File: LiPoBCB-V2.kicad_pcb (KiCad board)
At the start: 2 copper layers, 30 x 16.5 mm, 27 parts, among them J1 USB-C_6_pin_receptacle, J2 Conn_01x02, Q1 Q_Dual_PMOS_S1G1D2S2G2D1, U1 ETA9740

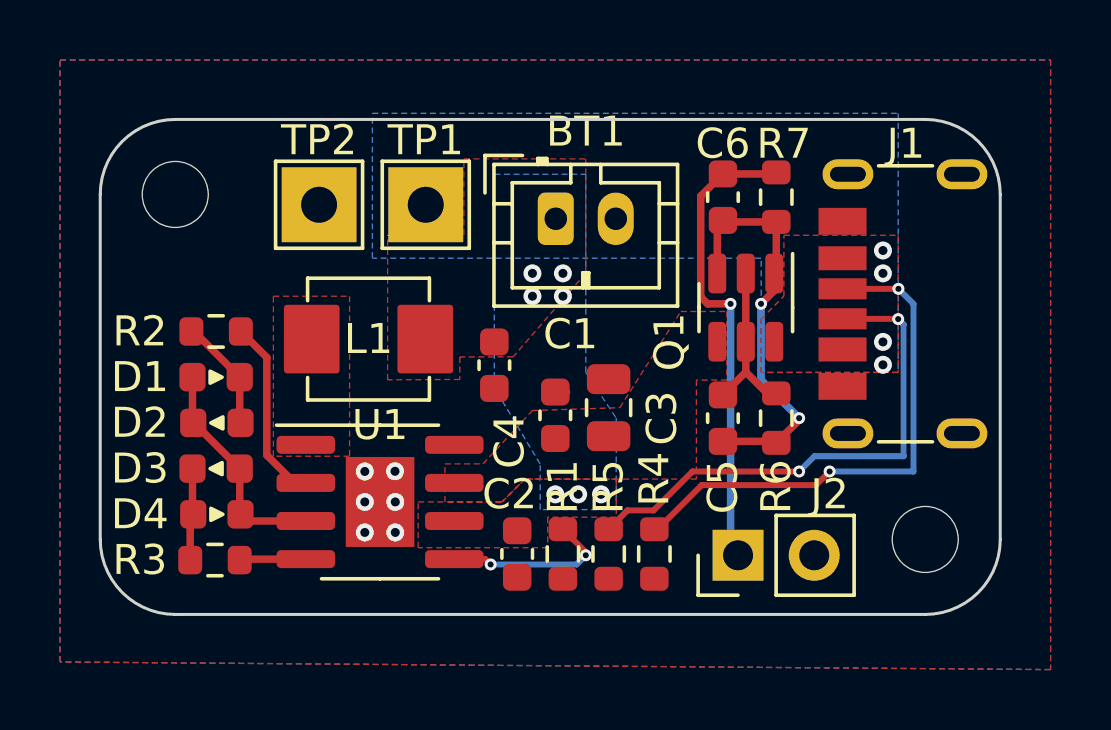
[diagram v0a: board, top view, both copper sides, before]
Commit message: DRC no errors
added 3d models
switched q1a and q1b
optimized polygons
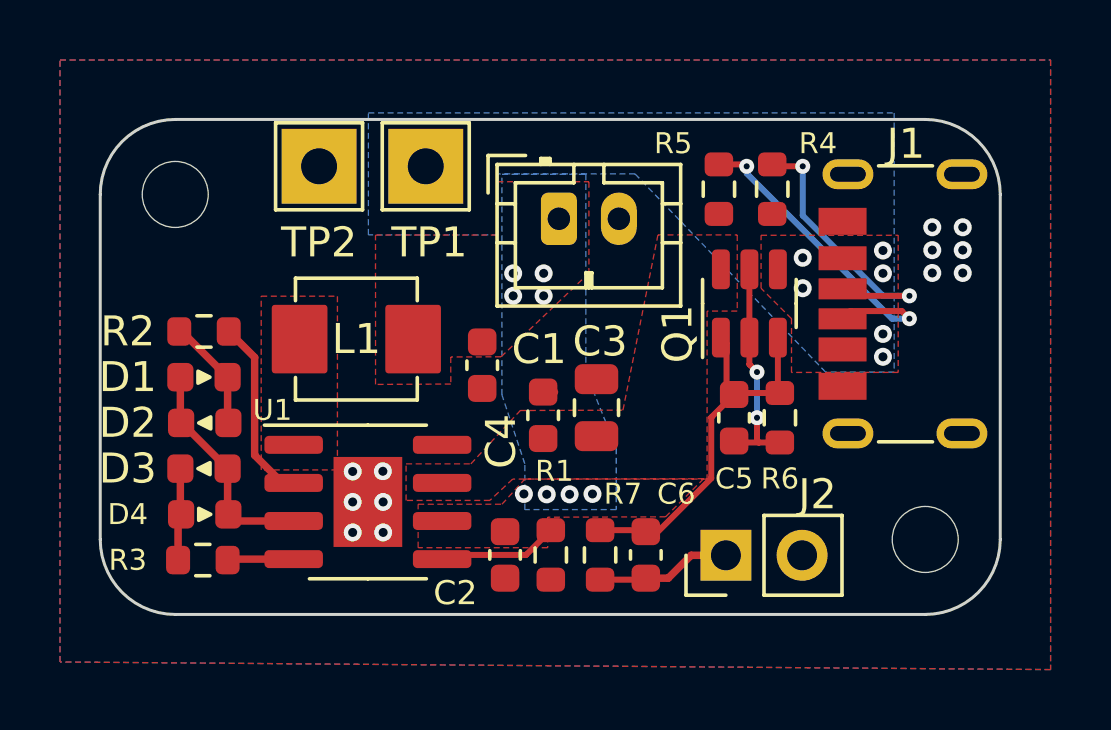
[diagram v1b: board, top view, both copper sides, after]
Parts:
- moved R7 13.3 mm to (146.7, 64.5), turned to -90 degrees
- moved R4 12.8 mm to (152.4, 52.3)
- moved R5 12.7 mm to (150.6, 52.3)
- moved C6 12.2 mm to (148.2, 64.5), turned to -90 degrees
- moved TP1 1.28 mm to (140.9, 51.6)
- moved TP2 1.28 mm to (137.3, 51.6)
- moved C2 0.41 mm to (143.5, 64.5)
- moved R1 0.41 mm to (145.0, 64.5)
- moved C3 0.40 mm to (146.5, 59.6)
- moved C4 0.40 mm to (142.7, 58.2)
- moved D2 0.40 mm to (133.5, 60.1)
- moved D4 0.40 mm to (133.5, 63.2)
- moved J2 0.40 mm to (150.9, 64.5)
- moved L1 0.40 mm to (138.5, 57.3)
- moved R3 0.40 mm to (133.4, 64.7)
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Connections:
- Q1 pad 4: +5V -> /VBUS
- Q1 pad 6: /VBUS -> +5V
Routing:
- net Net-(C6-Pad2): track 16.0 -> 4.53 mm, vias 1 -> 0
- net /CC2: track 17.6 -> 9.67 mm
- net /CC1: track 17.3 -> 11.1 mm
- net Net-(C5-Pad1): track 5.67 -> 7.45 mm, vias 0 -> 2
- net /ISET: track 5.77 -> 4.02 mm, vias 2 -> 0
- net /SW_GATE: track 13.9 -> 12.7 mm, vias 2 -> 0
- net GND: track 1.24 -> 0.37 mm, vias 6 -> 12
- net /VBUS: track 0.36 -> 0.00 mm, vias 4 -> 6
- net /BAT: track 0.35 -> 0.02 mm, vias 7 -> 8

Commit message: Updates design rules
edited inductor footprint
removed custom design rules
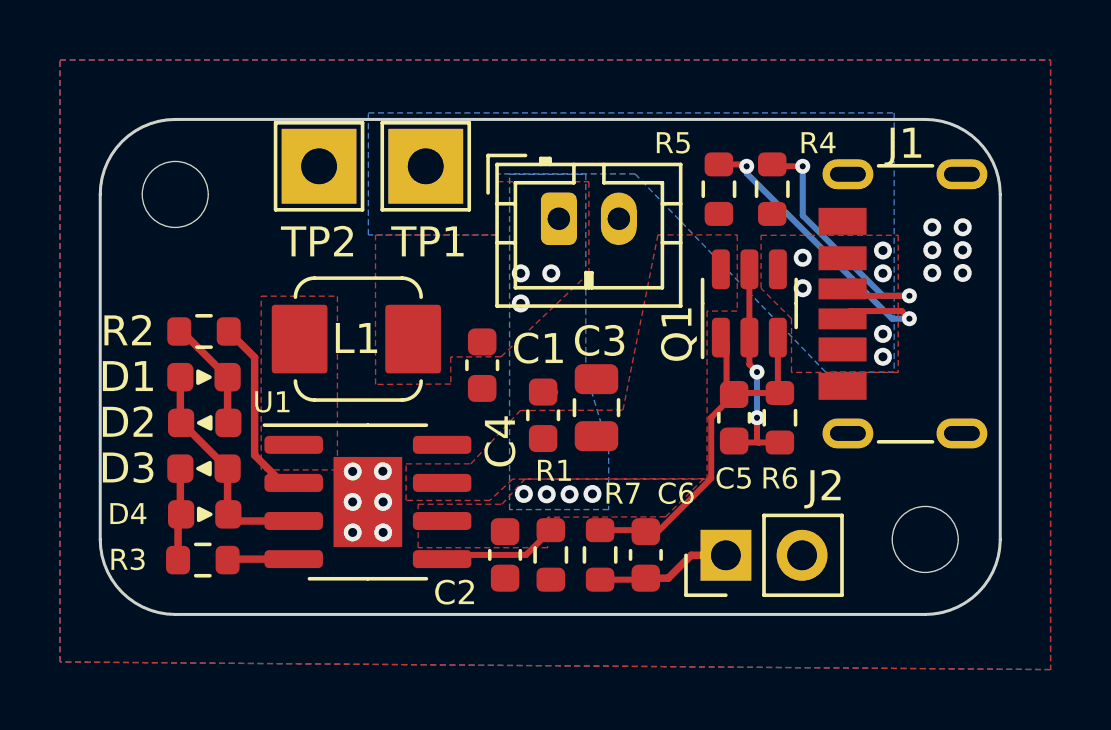
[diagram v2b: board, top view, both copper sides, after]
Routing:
- net /BAT: vias 8 -> 7
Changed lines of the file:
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@@
     (property "Sheetname" "")
     (attr through_hole)
-    (fp_text reference "J2" (at 2.032 3.053 180) (layer "F.SilkS")
+    (fp_text reference "J2" (at 2.298478 3.323 180) (layer "F.SilkS")
       (effects (font (size 1 1) (thickness 0.15)))
     )
@@
       (effects (font (size 1 1) (thickness 0.15)))
     )
-    (fp_line (start 2.03 2.03) (end 2.03 1.28) (layer "F.SilkS") (width 0.12))
-    (fp_line (start 2.03 -2.03) (end 2.03 -1.28) (layer "F.SilkS") (width 0.12))
-    (fp_line (start -2.03 2.03) (end -2.03 1.28) (layer "F.SilkS") (width 0.12))
-    (fp_line (start -2.03 -2.03) (end -2.03 -1.28) (layer "F.SilkS") (width 0.12))
-    (fp_line (start -2.03 2.03) (end 2.03 2.03) (layer "F.SilkS") (width 0.12))
-    (fp_line (start -2.03 -2.03) (end 2.03 -2.03) (layer "F.SilkS") (width 0.12))
+    (fp_line (start 1.524 2.032) (end -1.397 2.032) (layer "F.SilkS") (width 0.12))
+    (fp_line (start -1.397 -2.032) (end 1.524 -2.032) (layer "F.SilkS") (width 0.12))
+    (fp_arc (start 1.524 -2.032) (mid 1.973013 -1.846013) (end 2.159 -1.397) (layer "F.SilkS") (width 0.12))
+    (fp_arc (start 2.159 1.397) (mid 1.973013 1.846013) (end 1.524 2.032) (layer "F.SilkS") (width 0.12))
+    (fp_arc (start -2.032 -1.397) (mid -1.846013 -1.846013) (end -1.397 -2.032) (layer "F.SilkS") (width 0.12))
+    (fp_arc (start -1.397 2.032) (mid -1.846013 1.846013) (end -2.032 1.397) (layer "F.SilkS") (width 0.12))
     (fp_rect (start -3.175 -2.54) (end 3.175 2.54) (layer "F.CrtYd") (width 0.05) (fill none))
     (pad "1" smd roundrect (at -1.89225 0) (size 1.8545 2.286) (layers "F.Cu" "F.Paste" "F.Mask") (roundrect_rratio 0.05392289027)
@@
     (property "Sheetname" "")
     (attr smd)
-    (fp_text reference "U1" (at -3.182478 -3.060478) (layer "F.SilkS")
+    (fp_text reference "U1" (at -3.182478 -3.314478) (layer "F.SilkS")
       (effects (font (size 0.7 0.7) (thickness 0.15)))
     )
@@
   (segment (start 146.84075 60.636478) (end 146.91975 60.557478) (width 0.25) (layer "F.Cu") (net 3))
   (segment (start 142.745 57.670478) (end 142.732 57.657478) (width 0.25) (layer "F.Cu") (net 4))
-  (via (at 144.78 55.88) (size 0.6) (drill 0.3) (layers "F.Cu" "B.Cu") (free) (net 4))
   (via (at 144.121522 62.484) (size 0.6) (drill 0.3) (layers "F.Cu" "B.Cu") (free) (net 4))
-  (via (at 143.764 55.130478) (size 0.6) (drill 0.3) (layers "F.Cu" "B.Cu") (free) (net 4))
-  (via (at 144.78 55.130478) (size 0.6) (drill 0.3) (layers "F.Cu" "B.Cu") (free) (net 4))
-  (via (at 143.764 55.88) (size 0.6) (drill 0.3) (layers "F.Cu" "B.Cu") (free) (net 4))
+  (via (at 144.018 55.130478) (size 0.6) (drill 0.3) (layers "F.Cu" "B.Cu") (free) (net 4))
+  (via (at 145.034 55.130478) (size 0.6) (drill 0.3) (layers "F.Cu" "B.Cu") (free) (net 4))
+  (via (at 144.018 56.134) (size 0.6) (drill 0.3) (layers "F.Cu" "B.Cu") (free) (net 4))
   (via (at 146.407522 62.484) (size 0.6) (drill 0.3) (layers "F.Cu" "B.Cu") (free) (net 4))
   (via (at 145.645522 62.496478) (size 0.6) (drill 0.3) (layers "F.Cu" "B.Cu") (free) (net 4))
@@
       (pts
         (xy 146.184478 58.432478)
-        (xy 147.200478 60.96)
-        (xy 147.200478 63.004478)
-        (xy 144.152478 63.004478)
-        (xy 144.152478 61.480478)
-        (xy 143.390478 59.182)
-        (xy 143.390478 51.828478)
+        (xy 146.946478 60.96)
+        (xy 146.946478 63.004478)
+        (xy 143.644478 63.004478)
+        (xy 143.644478 61.480478)
+        (xy 143.644478 59.182)
+        (xy 143.644478 51.828478)
         (xy 146.184478 51.828478)
       )

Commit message: Adds new solder connector footprints
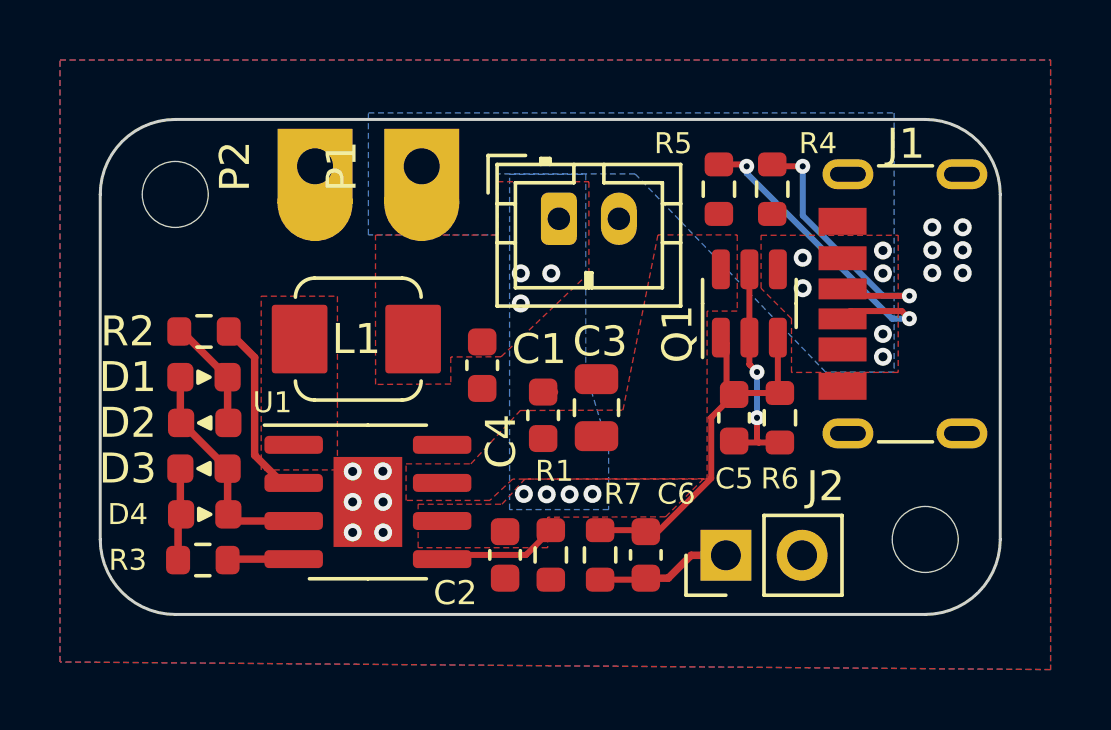
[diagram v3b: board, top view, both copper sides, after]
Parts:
- removed TP1: 5V, TestPoint:TestPoint_THTPad_2.5x2.5mm_Drill1.2mm
- removed TP2: GND, TestPoint:TestPoint_THTPad_2.5x2.5mm_Drill1.2mm
- added P1: Solder Pad, LiPoBCB-V2:TestPoint_THTPad_2.5x2.5mm_Drill1.2mm, F.Cu at (140.7, 51.6)
- added P2: Solder Pad, LiPoBCB-V2:TestPoint_THTPad_2.5x2.5mm_Drill1.2mm, F.Cu at (137.2, 51.6)
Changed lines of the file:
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@@
     )
-  )
-  (footprint "TestPoint:TestPoint_THTPad_2.5x2.5mm_Drill1.2mm" (layer "F.Cu")
-    (at 137.294478 51.562)
-    (descr "THT rectangular pad as test Point, square 2.5mm side length, hole diameter 1.2mm")
-    (tags "test point THT pad rectangle square")
-    (property "Sheetfile" "LiPoBCB-V2.kicad_sch")
-    (property "Sheetname" "")
-    (attr exclude_from_pos_files)
-    (fp_text reference "TP2" (at 0 2.54 180) (layer "F.SilkS")
-      (effects (font (size 1 1) (thickness 0.15)))
-    )
-    (fp_text value "GND" (at 0 2.25) (layer "F.Fab")
-      (effects (font (size 1 1) (thickness 0.15)))
-    )
-    (fp_text user "${REFERENCE}" (at 0 -2.15) (layer "F.Fab")
-      (effects (font (size 1 1) (thickness 0.15)))
-    )
-    (fp_line (start 1.45 -1.45) (end 1.45 1.45) (layer "F.SilkS") (width 0.12))
-    (fp_line (start -1.45 1.45) (end -1.45 -1.45) (layer "F.SilkS") (width 0.12))
-    (fp_line (start -1.45 -1.45) (end 1.45 -1.45) (layer "F.SilkS") (width 0.12))
-    (fp_line (start 1.45 1.45) (end -1.45 1.45) (layer "F.SilkS") (width 0.12))
-    (fp_line (start 1.75 1.75) (end -1.75 1.75) (layer "F.CrtYd") (width 0.05))
-    (fp_line (start -1.75 -1.75) (end 1.75 -1.75) (layer "F.CrtYd") (width 0.05))
-    (fp_line (start -1.75 -1.75) (end -1.75 1.75) (layer "F.CrtYd") (width 0.05))
-    (fp_line (start 1.75 1.75) (end 1.75 -1.75) (layer "F.CrtYd") (width 0.05))
-    (pad "1" thru_hole rect (at 0 0) (size 2.5 2.5) (drill 1.2) (layers *.Cu *.Mask)
-      (net 1 "GND") (pinfunction "1") (pintype "passive"))
   )
   (footprint "LiPoBCB-V2:D_0603_1608Metric" (layer "F.Cu")
@@
       (rotate (xyz 0 0 0))
     )
+  )
+  (footprint "LiPoBCB-V2:TestPoint_THTPad_2.5x2.5mm_Drill1.2mm" (layer "F.Cu")
+    (at 137.16 51.562)
+    (descr "THT rectangular pad as test Point, square 2.5mm side length, hole diameter 1.2mm")
+    (tags "test point THT pad rectangle square")
+    (property "Sheetfile" "LiPoBCB-V2.kicad_sch")
+    (property "Sheetname" "")
+    (attr exclude_from_pos_files)
+    (fp_text reference "P2" (at -2.667 0 270) (layer "F.SilkS")
+      (effects (font (size 1 1) (thickness 0.15)))
+    )
+    (fp_text value "Solder Pad" (at 0 5.08) (layer "F.Fab")
+      (effects (font (size 1 1) (thickness 0.15)))
+    )
+    (fp_text user "${REFERENCE}" (at -2.667 0 270) (layer "F.Fab")
+      (effects (font (size 1 1) (thickness 0.15)))
+    )
+    (fp_line (start -1.524 -1.524) (end 1.524 -1.524) (layer "F.CrtYd") (width 0.05))
+    (fp_line (start 1.524 1.239776) (end 1.524 -1.524) (layer "F.CrtYd") (width 0.05))
+    (fp_line (start -1.524 -1.524) (end -1.524034 1.25) (layer "F.CrtYd") (width 0.05))
+    (fp_arc (start 1.524 1.239776) (mid 0.005112 2.774026) (end -1.524034 1.25) (layer "F.CrtYd") (width 0.05))
+    (pad "1" thru_hole custom (at 0 0) (size 2.5 2.5) (drill 1.2) (layers *.Cu *.Mask)
+      (net 1 "GND") (pinfunction "1") (pintype "passive")
+      (options (clearance outline) (anchor rect))
+      (primitives
+        (gr_circle (center 0 1.24) (end 1.24 1.24) (width 0.02) (fill yes))
+      ))
   )
   (footprint "LiPoBCB-V2:D_0603_1608Metric" (layer "F.Cu")
@@
     )
   )
-  (footprint "TestPoint:TestPoint_THTPad_2.5x2.5mm_Drill1.2mm" (layer "F.Cu")
-    (at 140.850478 51.562)
-    (descr "THT rectangular pad as test Point, square 2.5mm side length, hole diameter 1.2mm")
-    (tags "test point THT pad rectangle square")
-    (property "Sheetfile" "LiPoBCB-V2.kicad_sch")
-    (property "Sheetname" "")
-    (attr exclude_from_pos_files)
-    (fp_text reference "TP1" (at 0.119522 2.54) (layer "F.SilkS")
-      (effects (font (size 1 1) (thickness 0.15)))
-    )
-    (fp_text value "5V" (at 0 2.25) (layer "F.Fab")
-      (effects (font (size 1 1) (thickness 0.15)))
-    )
-    (fp_text user "${REFERENCE}" (at 0 -2.15) (layer "F.Fab")
-      (effects (font (size 1 1) (thickness 0.15)))
-    )
-    (fp_line (start 1.45 1.45) (end -1.45 1.45) (layer "F.SilkS") (width 0.12))
-    (fp_line (start 1.45 -1.45) (end 1.45 1.45) (layer "F.SilkS") (width 0.12))
-    (fp_line (start -1.45 -1.45) (end 1.45 -1.45) (layer "F.SilkS") (width 0.12))
-    (fp_line (start -1.45 1.45) (end -1.45 -1.45) (layer "F.SilkS") (width 0.12))
-    (fp_line (start 1.75 1.75) (end 1.75 -1.75) (layer "F.CrtYd") (width 0.05))
-    (fp_line (start -1.75 -1.75) (end 1.75 -1.75) (layer "F.CrtYd") (width 0.05))
-    (fp_line (start 1.75 1.75) (end -1.75 1.75) (layer "F.CrtYd") (width 0.05))
-    (fp_line (start -1.75 -1.75) (end -1.75 1.75) (layer "F.CrtYd") (width 0.05))
-    (pad "1" thru_hole rect (at 0 0) (size 2.5 2.5) (drill 1.2) (layers *.Cu *.Mask)
-      (net 16 "/VBUS") (pinfunction "1") (pintype "passive"))
-  )
   (footprint "Capacitor_SMD:C_0805_2012Metric" (layer "F.Cu")
     (at 146.542 59.607478 90)
@@
     )
   )
+  (footprint "LiPoBCB-V2:TestPoint_THTPad_2.5x2.5mm_Drill1.2mm" (layer "F.Cu")
+    (at 140.716 51.562)
+    (descr "THT rectangular pad as test Point, square 2.5mm side length, hole diameter 1.2mm")
+    (tags "test point THT pad rectangle square")
+    (property "Sheetfile" "LiPoBCB-V2.kicad_sch")
+    (property "Sheetname" "")
+    (attr exclude_from_pos_files)
+    (fp_text reference "P1" (at -2.667 0 270) (layer "F.SilkS")
+      (effects (font (size 1 1) (thickness 0.15)))
+    )
+    (fp_text value "Solder Pad" (at 0 5.08) (layer "F.Fab")
+      (effects (font (size 1 1) (thickness 0.15)))
+    )
+    (fp_text user "${REFERENCE}" (at -2.667 0 270) (layer "F.Fab")
+      (effects (font (size 1 1) (thickness 0.15)))
+    )
+    (fp_line (start -1.524 -1.524) (end 1.524 -1.524) (layer "F.CrtYd") (width 0.05))
+    (fp_line (start 1.524 1.239776) (end 1.524 -1.524) (layer "F.CrtYd") (width 0.05))
+    (fp_line (start -1.524 -1.524) (end -1.524034 1.25) (layer "F.CrtYd") (width 0.05))
+    (fp_arc (start 1.524 1.239776) (mid 0.005112 2.774026) (end -1.524034 1.25) (layer "F.CrtYd") (width 0.05))
+    (pad "1" thru_hole custom (at 0 0) (size 2.5 2.5) (drill 1.2) (layers *.Cu *.Mask)
+      (net 16 "/VBUS") (pinfunction "1") (pintype "passive")
+      (options (clearance outline) (anchor rect))
+      (primitives
+        (gr_circle (center 0 1.24) (end 1.24 1.24) (width 0.02) (fill yes))
+      ))
+  )
   (footprint "LiPoBCB-V2:L_smd_1616" (layer "F.Cu")

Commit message: Adds silkscreen to the back
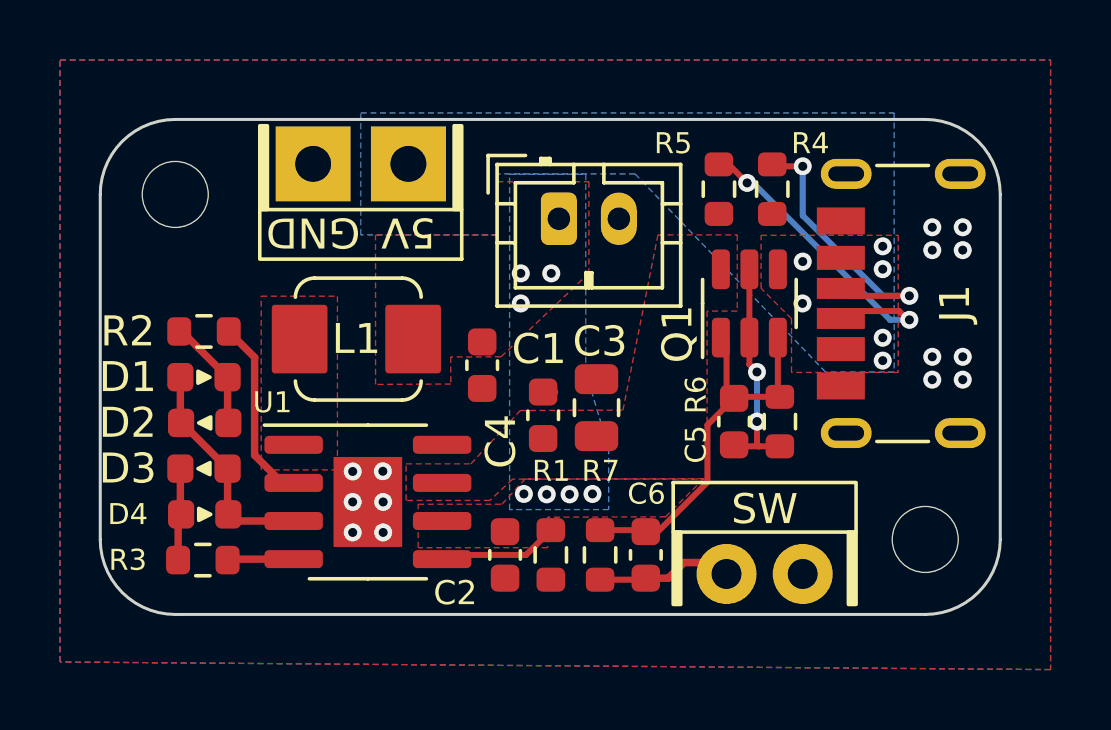
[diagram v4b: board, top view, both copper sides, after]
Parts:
- removed P2: Solder Pad, LiPoBCB-V2:TestPoint_THTPad_2.5x2.5mm_Drill1.2mm
- J2: footprint Connector_PinHeader_2.54mm:PinHeader_1x02_P2.54mm_Vertical -> LiPoBCB-V2:Solder_Connector_SW
- P1: value Solder Pad -> Solder_Connector_X2; footprint LiPoBCB-V2:TestPoint_THTPad_2.5x2.5mm_Drill1.2mm -> LiPoBCB-V2:Solder_Connector_X2
- moved J2 0.62 mm to (150.9, 65.2), turned to 0 degrees
- moved P1 0.45 mm to (140.3, 51.5), turned to 180 degrees
- moved C5 0.13 mm to (151.1, 60.1)
- moved R6 0.13 mm to (152.7, 60.1)
- moved J1 0.06 mm to (154.7, 56.1)
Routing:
- net GND: vias 12 -> 14
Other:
- board text added: "LiPoBCB V2.0 Jakob Holz - 03.12.22"
- board text added: "max.2A"
- board text added: "on/off"
